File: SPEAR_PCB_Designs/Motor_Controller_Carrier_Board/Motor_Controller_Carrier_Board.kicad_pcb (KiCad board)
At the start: 2 copper layers, 101 x 71 mm, 15 parts, among them J1 Conn_01x02_Pin, J2 Conn_01x02_Pin, J3 Conn_01x02_Pin, J4 JST_S4B-XH-A-1, U1 AP63203WU

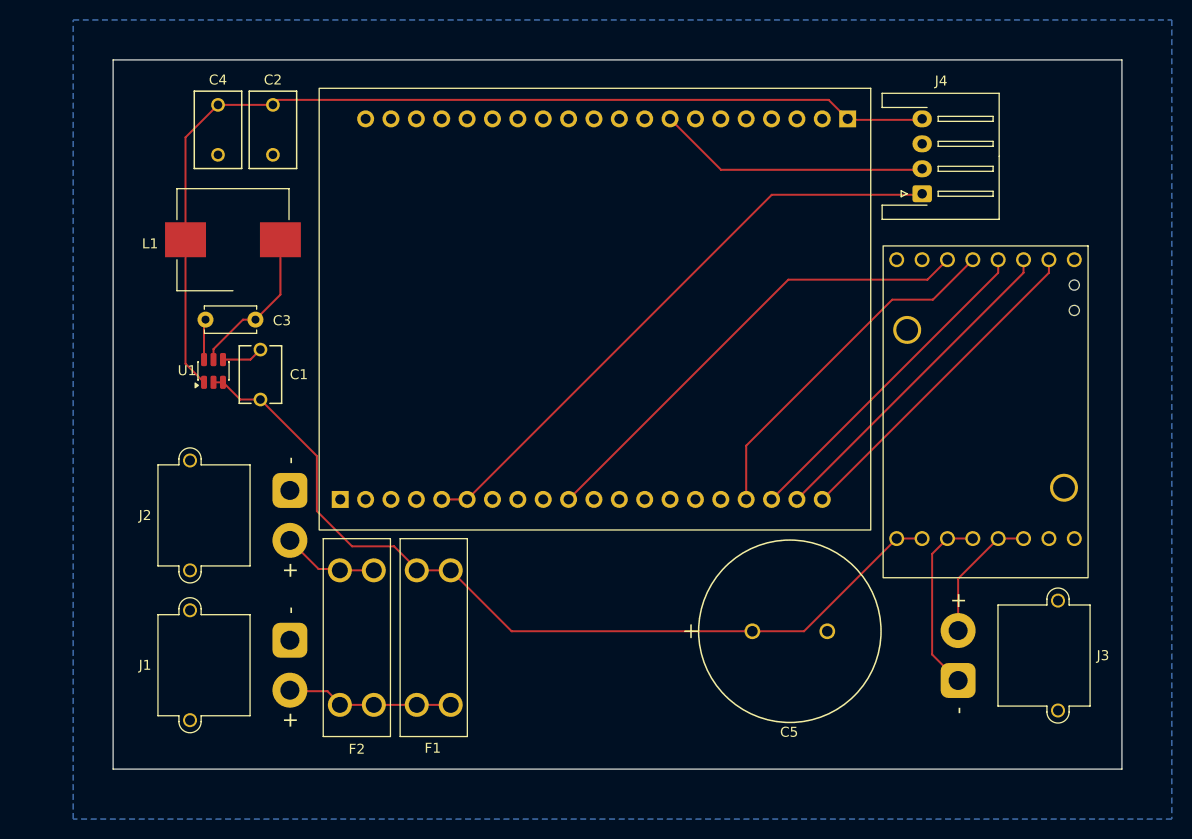
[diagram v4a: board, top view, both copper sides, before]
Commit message: Started redesigning the carrier board to have the correct dimensions
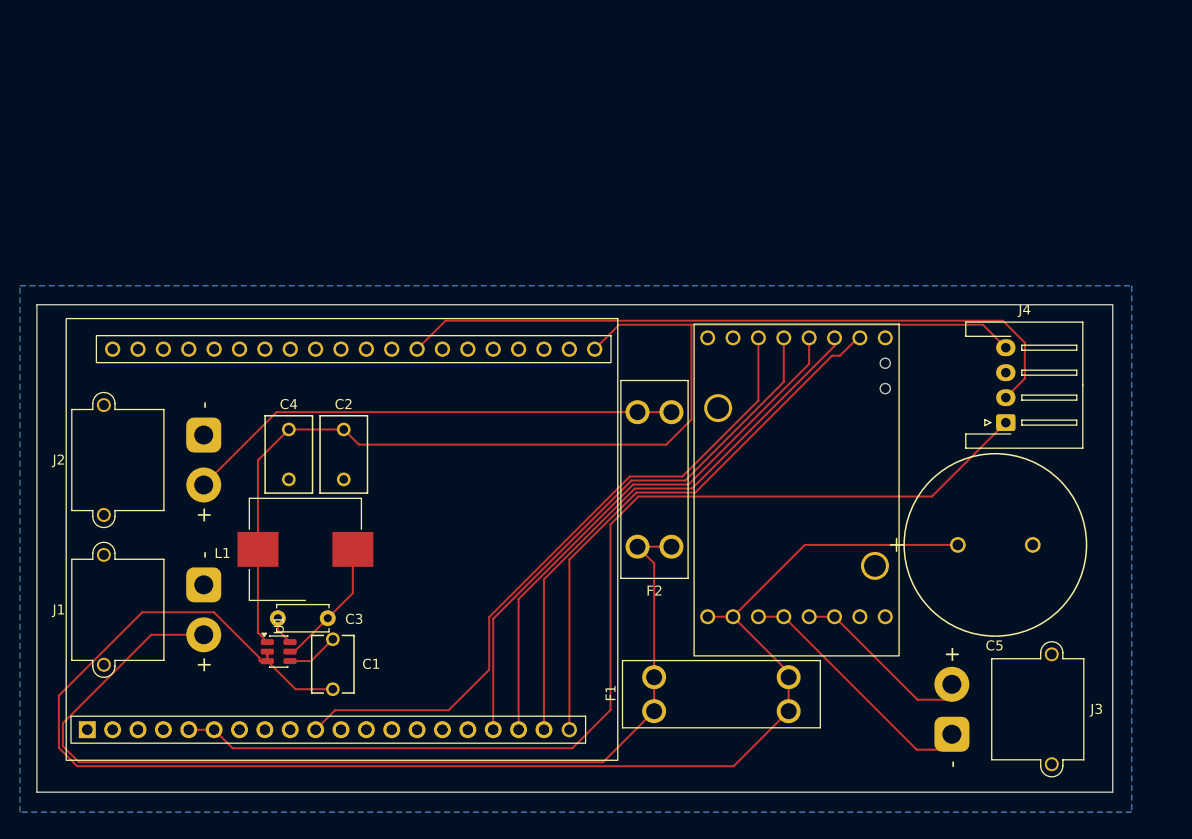
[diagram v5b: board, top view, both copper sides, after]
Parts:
- moved MCB1 34.2 mm to (142.4, 73.0)
- moved F2 33.7 mm to (146.2, 89.0)
- moved C2 33.3 mm to (115.1, 84.0)
- moved C4 33.3 mm to (109.6, 84.0)
- moved L1 31.8 mm to (111.2, 96.0)
- moved C3 30.8 mm to (113.5, 102.9)
- moved C1 29.9 mm to (114.0, 110.0)
- moved F1 29.4 mm to (152.9, 110.5), turned to 0 degrees
- moved U1 28.8 mm to (108.6, 106.2), turned to 0 degrees
- moved J4 24.4 mm to (181.4, 83.3)
- moved C5 22.3 mm to (176.6, 95.6)
- moved MDB1 20.5 mm to (170.6, 73.6)
- moved J1 10.3 mm to (101.1, 99.6)
- moved J2 10.3 mm to (101.1, 84.6)
- moved J3 5.42 mm to (176.0, 114.5)
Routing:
- net Net-(J1-Pin_2): track 16.8 -> 102.6 mm
- net +BATT: track 88.4 -> 157.4 mm
- net /ENC_B: track 60.8 -> 107.0 mm
- net /ENC_A: track 27.4 -> 69.2 mm
- net Net-(J2-Pin_2): track 9.64 -> 49.8 mm
- net /DIR: track 33.4 -> 55.3 mm
- net /PWM: track 33.4 -> 54.6 mm
- net /SLP: track 33.4 -> 54.5 mm
- net /CS: track 47.9 -> 67.3 mm
- net /FLT: track 35.8 -> 54.4 mm
- net +3.3V: track 101.5 -> 117.6 mm
- net Net-(J3-Pin_1): track 18.5 -> 26.4 mm
- net Net-(J3-Pin_2): track 13.4 -> 19.3 mm
- net /SW: track 15.5 -> 13.1 mm
- net Net-(U1-BST): track 4.06 -> 2.90 mm
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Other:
- board size 101 x 71 mm -> 107.7 x 48.8 mm

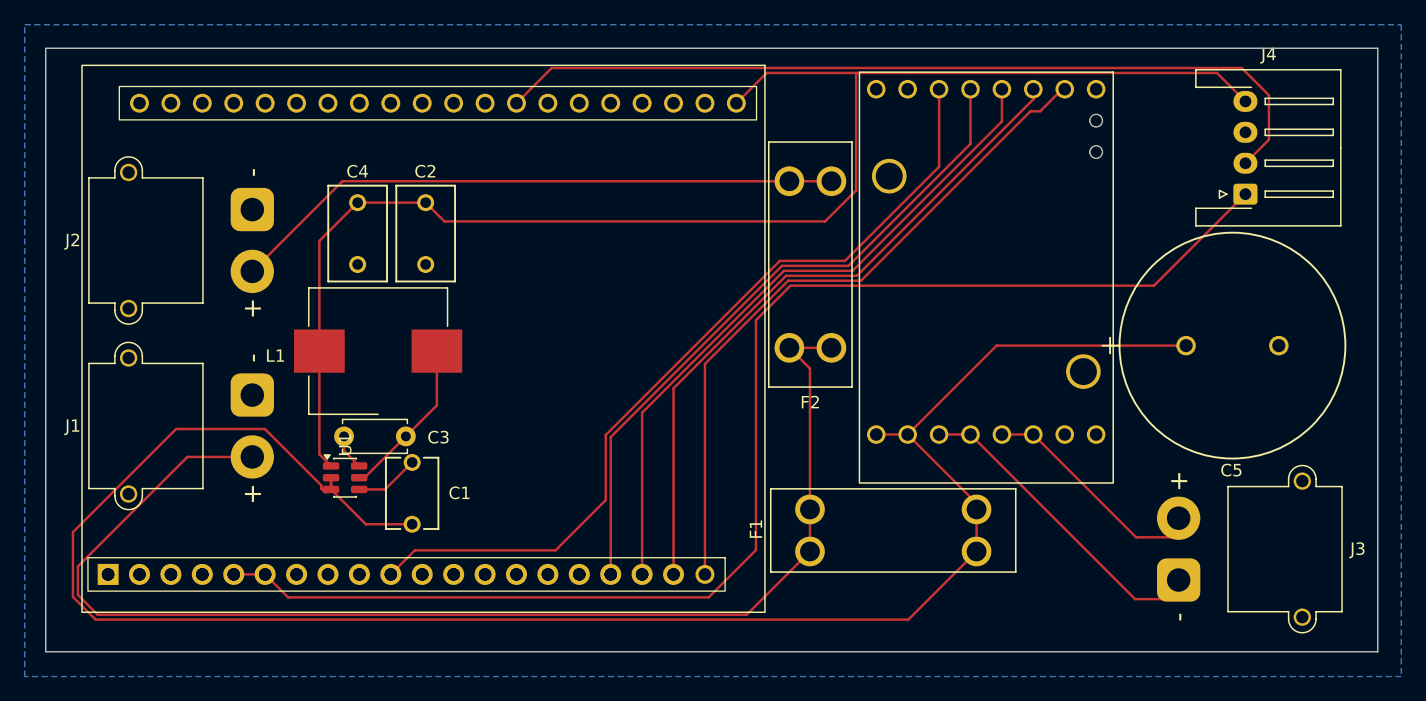
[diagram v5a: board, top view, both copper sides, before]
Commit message: Moved power traces to the back for carrier board
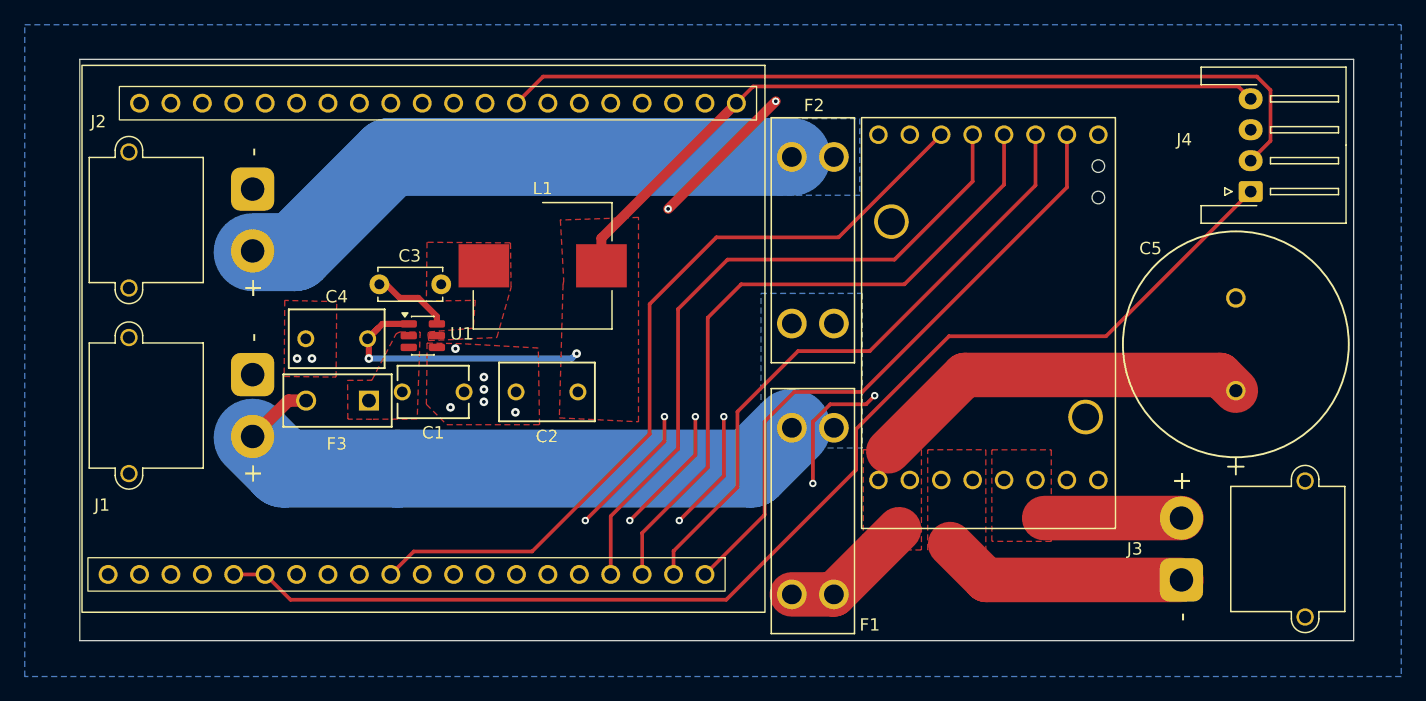
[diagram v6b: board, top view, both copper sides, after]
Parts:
- added F3: Fuse, Motor_Controller_Carrier_Board:FUS_LITTELFUSE_392_LTF, F.Cu at (110.5, 100.0)
- moved C2 19.6 mm to (127.4, 99.3), turned to 180 degrees
- moved L1 15.0 mm to (124.5, 89.1), turned to 0 degrees
- moved U1 13.1 mm to (114.9, 94.8)
- moved C3 12.6 mm to (116.3, 90.6)
- moved C4 11.0 mm to (110.4, 95.0), turned to 180 degrees
- moved C1 10.7 mm to (113.2, 99.3), turned to 0 degrees
- moved F1 6.69 mm to (146.4, 108.9), turned to -90 degrees
- moved C5 5.43 mm to (180.6, 99.2), turned to 90 degrees
- moved MDB1 3.68 mm to (170.8, 77.2)
- moved F2 1.98 mm to (146.4, 87.0)
- moved J1 1.66 mm to (101.1, 97.9)
- moved J2 1.66 mm to (101.1, 82.9)
- moved J4 0.47 mm to (181.8, 83.1)
- moved J3 0.23 mm to (176.2, 114.5)
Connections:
- C1 pad 1: +BATT -> /BUCK_PWR
- C5 pad 1: +BATT -> /DRIVER_PWR
- F1 pad 2_1: +BATT -> /DRIVER_PWR
- F1 pad 2_2: +BATT -> /DRIVER_PWR
- MDB1 pad 15: +BATT -> /DRIVER_PWR
- MDB1 pad 16: +BATT -> /DRIVER_PWR
- U1 pad 2: +BATT -> /BUCK_PWR
- U1 pad 3: +BATT -> /BUCK_PWR
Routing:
- net +BATT: track 157.4 -> 0.00 mm
- net Net-(J1-Pin_2): track 102.6 -> 51.5 mm
- net GND: track 5.19 -> 54.7 mm, vias 0 -> 18
- net /DRIVER_PWR: track 0.00 -> 42.0 mm
- net +3.3V: track 117.6 -> 83.7 mm, vias 0 -> 2
- net /SW: track 13.1 -> 0.00 mm
- net /ENC_B: track 107.0 -> 98.7 mm
- net Net-(J3-Pin_2): track 19.3 -> 11.1 mm
- net Net-(J3-Pin_1): track 26.4 -> 19.9 mm
- net /DIR: track 55.3 -> 50.9 mm
- net /PWM: track 54.6 -> 51.1 mm
- net Net-(U1-BST): track 2.90 -> 6.33 mm
- net Net-(J2-Pin_2): track 49.8 -> 46.8 mm
- net /CS: track 67.3 -> 65.4 mm
- net /FLT: track 54.4 -> 55.6 mm
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- added copper zone on F.Cu, net +3.3V
- added copper zone on F.Cu, net /BUCK_PWR
- added copper zone on F.Cu, net /DRIVER_PWR
- added copper zone on F.Cu, net /SW
- added copper zone on F.Cu, net GND
- added copper zone on B.Cu, net Net-(J1-Pin_2)
- added copper zone on B.Cu, net Net-(J2-Pin_2)
- added copper zone on F.Cu, net Net-(J3-Pin_1)
- added copper zone on F.Cu, net Net-(J3-Pin_2)
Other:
- board size 107.7 x 48.8 mm -> 103 x 47 mm

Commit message: Moved power traces to the front and made minor adjustments to the layout of the carrier board
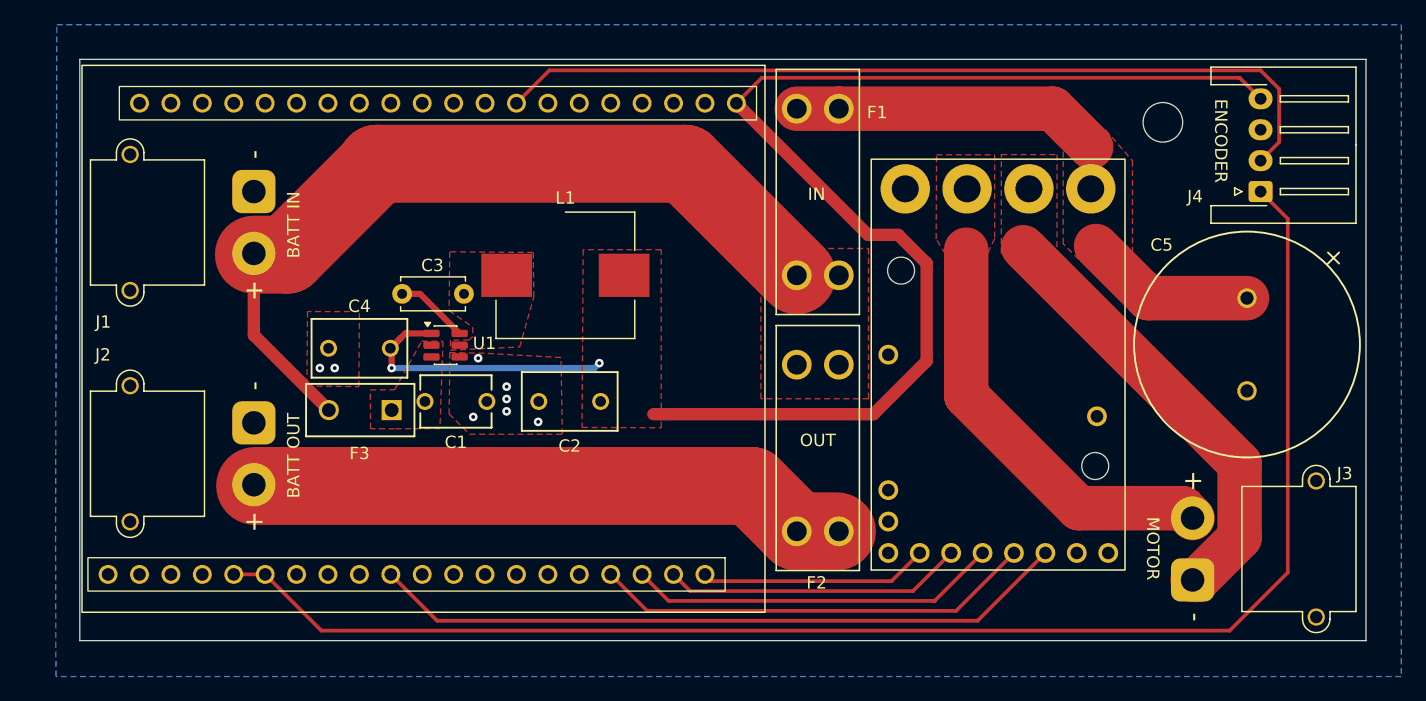
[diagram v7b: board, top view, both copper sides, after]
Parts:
- added REF**: MountingHole_3.2mm_M3, MountingHole:MountingHole_3.2mm_M3, F.Cu at (174.7, 77.5)
- moved MDB1 41.3 mm to (151.2, 113.6), turned to 90 degrees
- moved F1 25.8 mm to (146.8, 83.1), turned to 90 degrees
- moved J2 18.9 mm to (101.2, 101.8)
- moved F2 16.8 mm to (146.8, 103.8), turned to -90 degrees
- moved J1 14.8 mm to (101.2, 83.1)
- moved C5 7.54 mm to (181.5, 91.7), turned to -90 degrees
- moved C3 1.99 mm to (118.2, 91.4)
- moved L1 1.99 mm to (126.4, 89.9)
- moved F3 1.99 mm to (112.3, 100.8)
- moved U1 1.99 mm to (116.7, 95.5)
- moved C1 1.99 mm to (115.0, 100.1)
- moved C2 1.99 mm to (129.2, 100.1)
- moved C4 1.99 mm to (112.2, 95.8)
- moved J3 0.90 mm to (177.1, 114.5)
- moved J4 0.80 mm to (182.6, 83.1)
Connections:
- MDB1 pad 10: GND -> unconnected-(MDB1-VREF-Pad10)
- MDB1 pad 11: Net-(J3-Pin_2) -> GND
- MDB1 pad 14: Net-(J3-Pin_1) -> /DRIVER_PWR
- MDB1 pad 15: /DRIVER_PWR -> GND
- MDB1 pad 16: /DRIVER_PWR -> GND
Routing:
- net GND: track 54.7 -> 0.00 mm, vias 18 -> 8
- net +3.3V: track 83.7 -> 120.0 mm
- net /DIR: track 50.9 -> 18.5 mm
- net /PWM: track 51.1 -> 24.3 mm
- net /SLP: track 55.4 -> 30.0 mm
- net Net-(J3-Pin_2): track 11.1 -> 34.2 mm
- net /ENC_B: track 98.7 -> 120.8 mm
- net /FLT: track 55.6 -> 35.8 mm
- net Net-(J3-Pin_1): track 19.9 -> 35.9 mm
- net Net-(J1-Pin_2): track 51.5 -> 65.9 mm
- net /CS: track 65.4 -> 56.7 mm
- net /DRIVER_PWR: track 42.0 -> 39.0 mm
- net Net-(J2-Pin_2): track 46.8 -> 48.6 mm
- net /ENC_A: track 68.7 -> 69.8 mm
- added copper zone on F.Cu, net Net-(J1-Pin_2)
- removed copper zone on B.Cu, net Net-(J1-Pin_2)
- removed copper zone on B.Cu, net Net-(J2-Pin_2)
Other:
- board size 103 x 47 mm -> 104 x 47 mm
- board text added: "BATT IN"
- board text added: "BATT OUT"
- board text added: "ENCODER"
- board text added: "IN"
- board text added: "MOTOR"
- board text added: "OUT"

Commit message: Almost finished getting carrier board ready for fabrication
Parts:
- added G***: LOGO, SPEAR_Logos:spear_logo_10.0x10, B.Cu at (122.6, 80.3)
- C3: footprint Capacitor_THT:C_Disc_D5.0mm_W2.5mm_P5.00mm -> Motor_Controller_Carrier_Board:C_Disc_D5.0mm_W2.5mm_P5.00mm
- J1, J2, J3: footprint Connector_AMASS:AMASS_XT30PW-M_1x02_P2.50mm_Horizontal -> SPEAR_Connectors:AMASS_XT30PW-M_1x02_P2.50mm_Horizontal_1
- J4: footprint Connector_JST:JST_XH_S4B-XH-A-1_1x04_P2.50mm_Horizontal -> SPEAR_Connectors:JST_XH_S4B-XH-A-1_1x04_P2.50mm_Horizontal
- U1: footprint Package_TO_SOT_SMD:TSOT-23-6 -> Motor_Controller_Carrier_Board:TSOT-23-6
- moved C3 9.46 mm to (114.4, 82.7), turned to -90 degrees
- moved C4 4.28 mm to (109.7, 92.3)
- moved C5 4.02 mm to (179.4, 88.3)
- moved F1 4.02 mm to (144.7, 79.7)
- moved L1 4.02 mm to (124.3, 86.5)
- moved MDB1 4.02 mm to (149.1, 110.2)
- moved C2 4.02 mm to (127.1, 96.7)
- moved F2 4.02 mm to (144.7, 100.4)
- moved F3 4.02 mm to (110.2, 97.4)
- moved J1 4.02 mm to (99.1, 79.7)
- moved J2 4.02 mm to (99.1, 98.4)
- moved J3 4.02 mm to (175.0, 111.1)
- moved J4 4.02 mm to (180.5, 79.7)
- moved MCB1 4.02 mm to (140.3, 69.6)
- moved REF** 4.02 mm to (172.6, 74.1)
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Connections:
- MDB1 pad 12: Net-(J3-Pin_2) -> GND
- MDB1 pad 13: Net-(J3-Pin_1) -> GND
- MDB1 pad 14: /DRIVER_PWR -> GND
- MDB1 pad 16: GND -> Net-(J3-Pin_2)
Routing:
- net Net-(U1-BST): track 5.98 -> 4.00 mm
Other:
- outline, holes or cut-outs redrawn
- board text added: "2992"
- board text added: "Oliver Schneider Ronak Grover Henry Diep"
- board text added: "Version 1.0"
